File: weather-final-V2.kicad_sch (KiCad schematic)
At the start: 41 parts, among them J1 Conn_02x04_Odd_Even, J2 Conn_01x06_Pin, J3 PROGRAMMING_CONN, J4 USB_C_Receptacle_PowerOnly_6P, U1 AMS1117-5.0, U2 ATmega328-P, Y1 Crystal

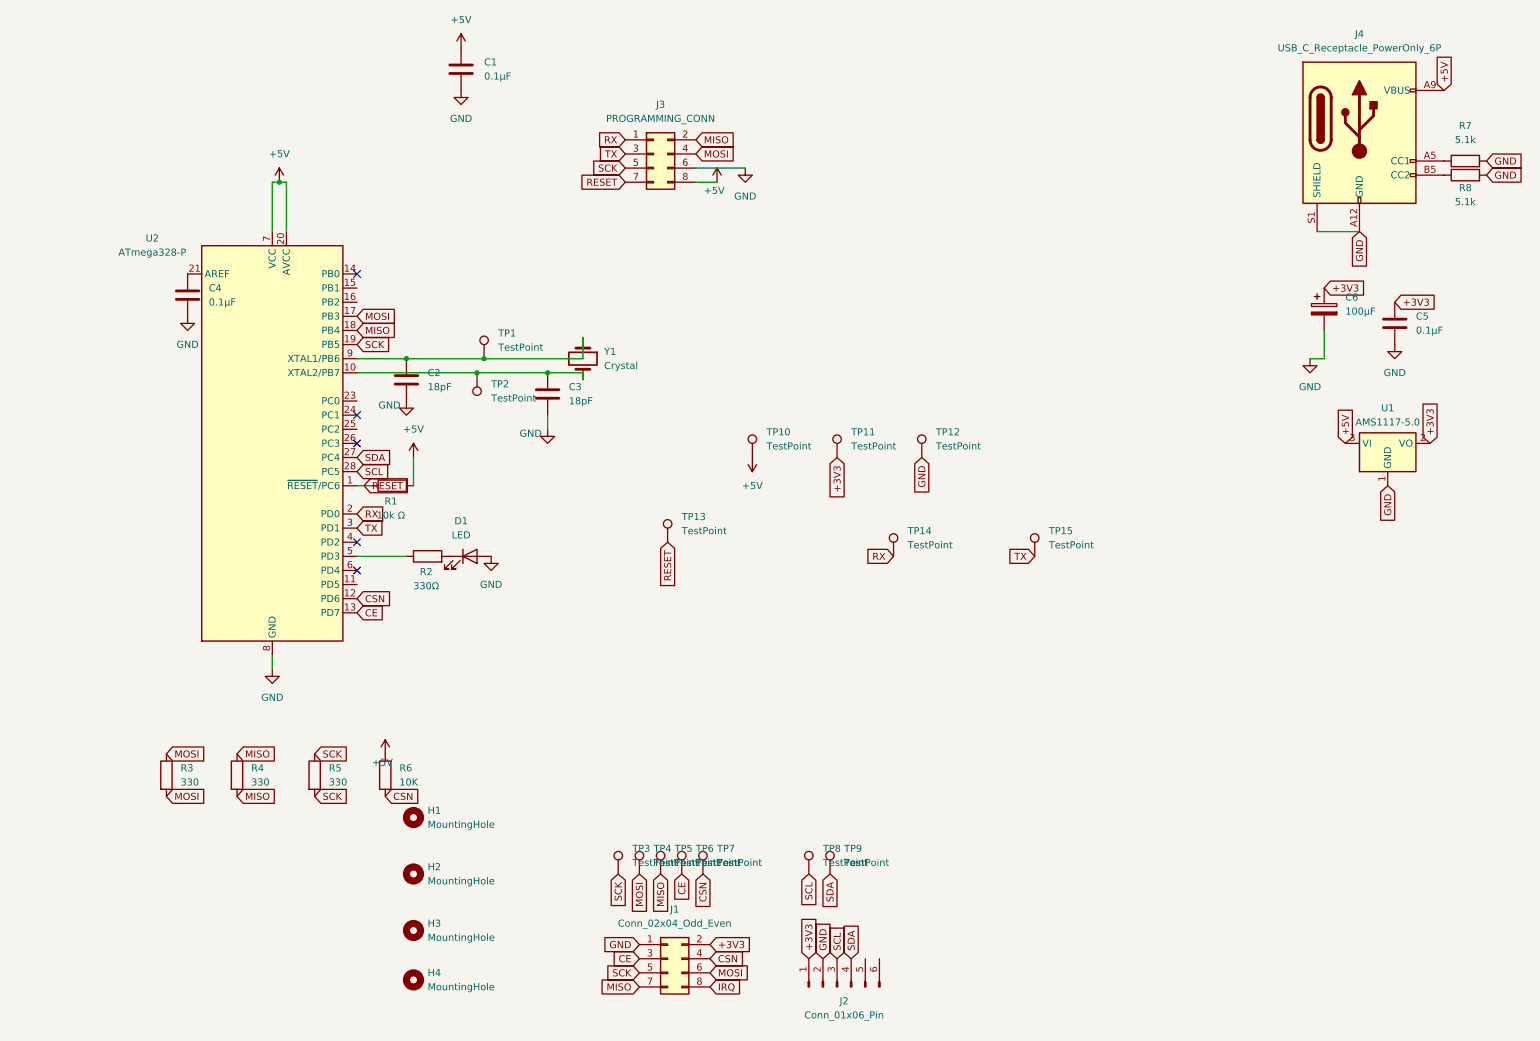
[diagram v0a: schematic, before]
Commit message: Add i2c pullups Clean unnecessary trace widths Add diode for reverse voltage protection on J3 input
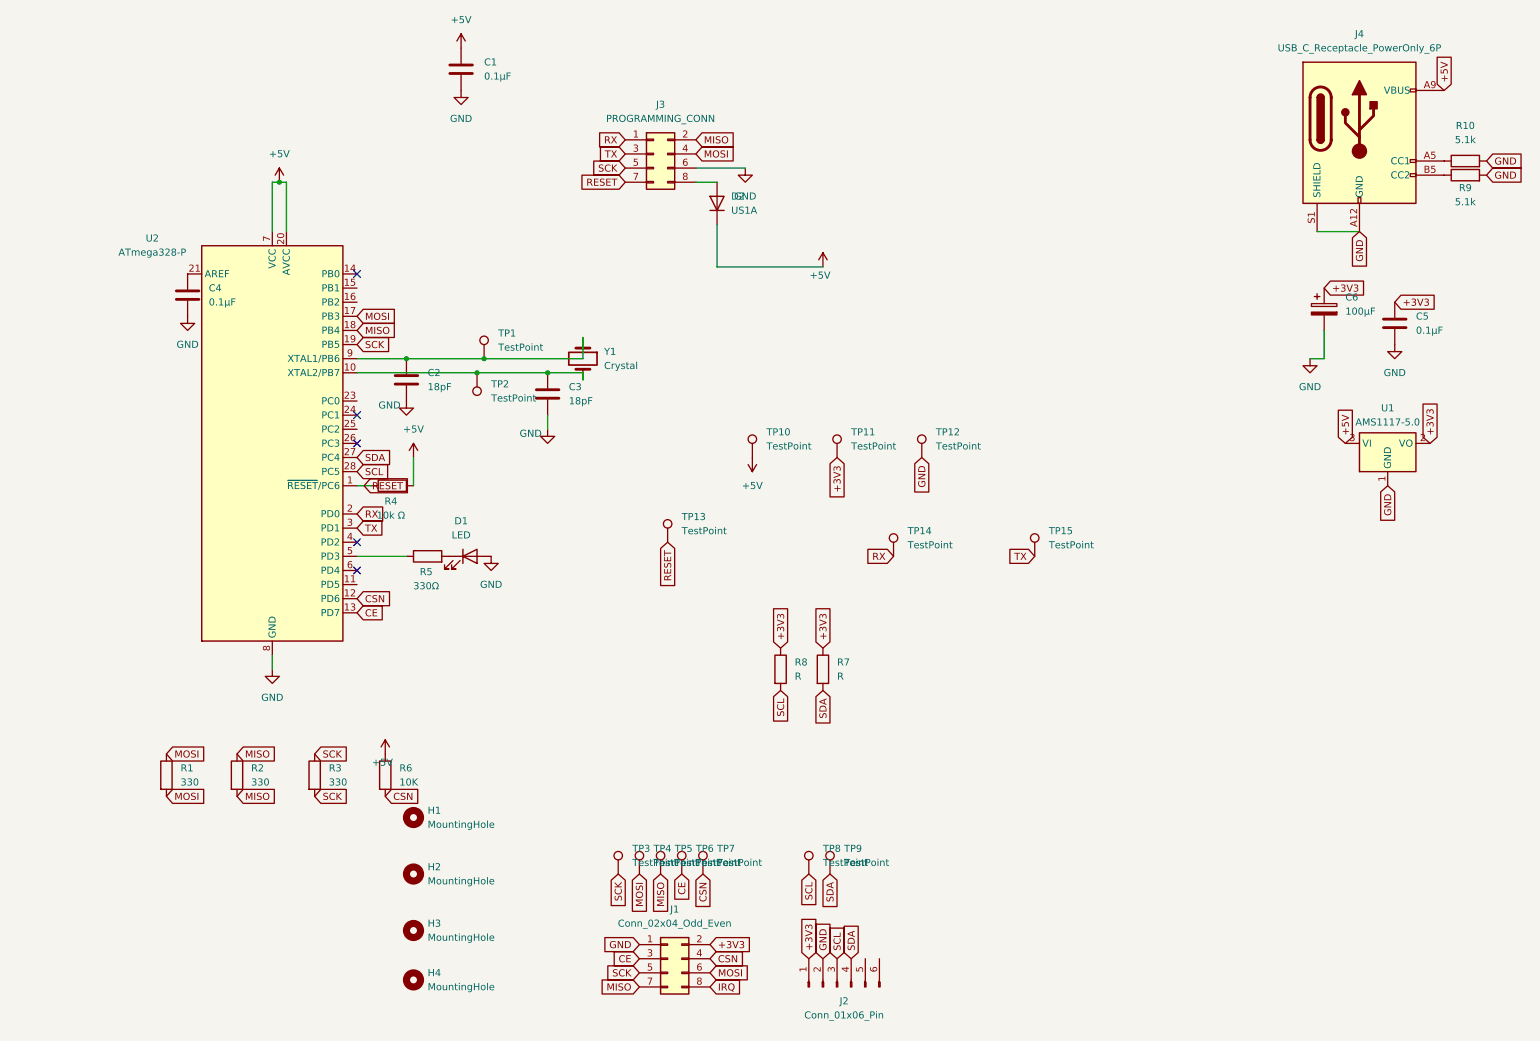
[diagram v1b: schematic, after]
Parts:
- added D2: US1A, Diode_SMD:D_SMA, symbol Diode:US1A
- added R7, R8: R, Resistor_SMD:R_1206_3216Metric_Pad1.30x1.75mm_HandSolder, symbol Device:R
- renumbered R3 to R1, R7 to R10, R4 to R2, R5 to R3, R1 to R4, R2 to R5, R8 to R9
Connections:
- net +3V3: now also R7.1, R8.1
- net +5V: now also D2.1 (K); no longer J3.8 (Pin_8)
- net SCL: now also R8.2
- net SDA: now also R7.2
- new net: D2.2 (A), J3.8 (Pin_8)

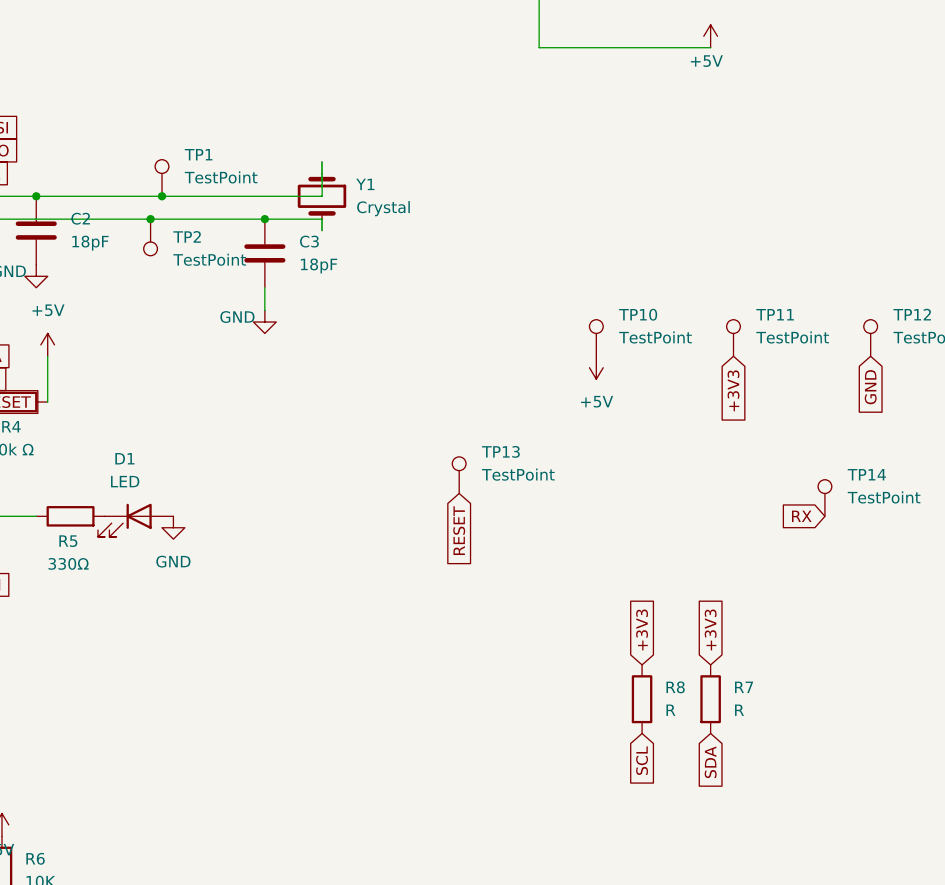
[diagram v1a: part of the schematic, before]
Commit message: Add i2c pullup resistors' values Fix a silkscreen overlap
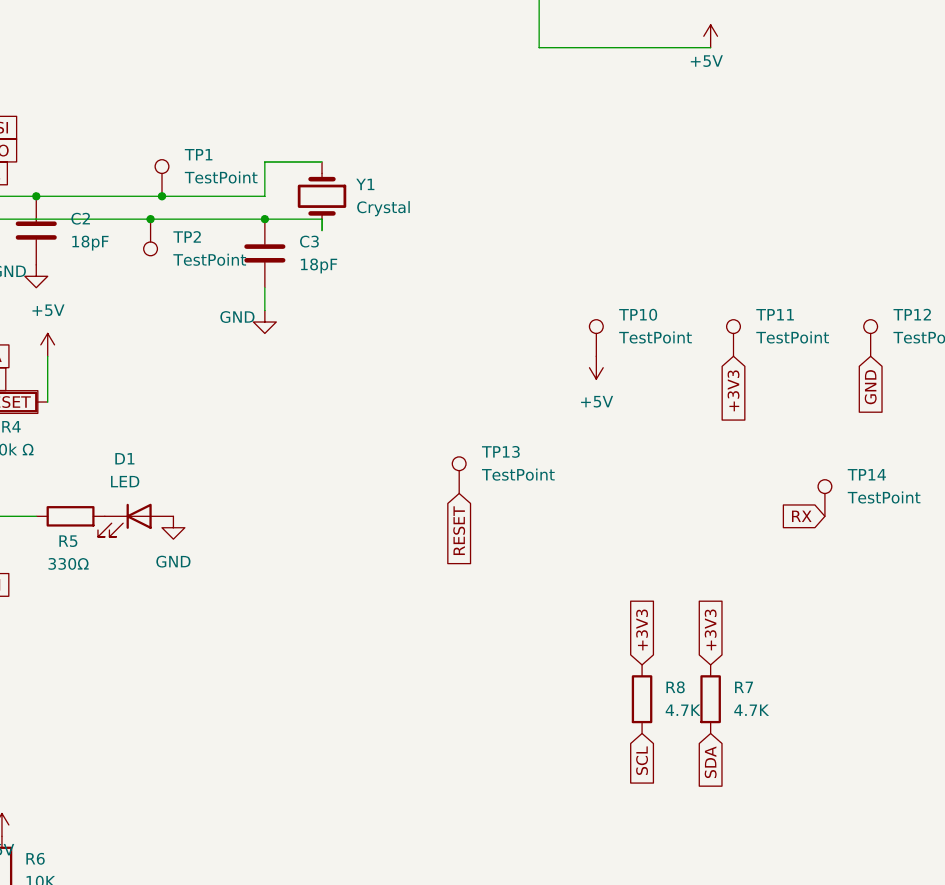
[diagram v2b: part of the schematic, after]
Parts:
- R7, R8: value R -> 4.7K
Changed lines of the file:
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@@
 	(wire
 		(pts
-			(xy 115.57 76.2) (xy 115.57 72.39)
+			(xy 115.57 72.39) (xy 109.22 72.39)
 		)
 		(stroke
@@
 	(wire
 		(pts
-			(xy 97.79 76.2) (xy 115.57 76.2)
+			(xy 109.22 72.39) (xy 109.22 76.2)
 		)
 		(stroke
@@
 	(wire
 		(pts
+			(xy 109.22 76.2) (xy 97.79 76.2)
+		)
+		(stroke
+			(width 0)
+			(type default)
+		)
+	)
+	(wire
+		(pts
 			(xy 247.65 53.34) (xy 255.27 53.34)
 		)
@@
 			)
 		)
-		(property "Value" "R"
+		(property "Value" "4.7K"
 			(at 161.29 133.3499 0)
 			(effects
@@
 			)
 		)
-		(property "Value" "R"
+		(property "Value" "4.7K"
 			(at 153.67 133.3499 0)
 			(effects

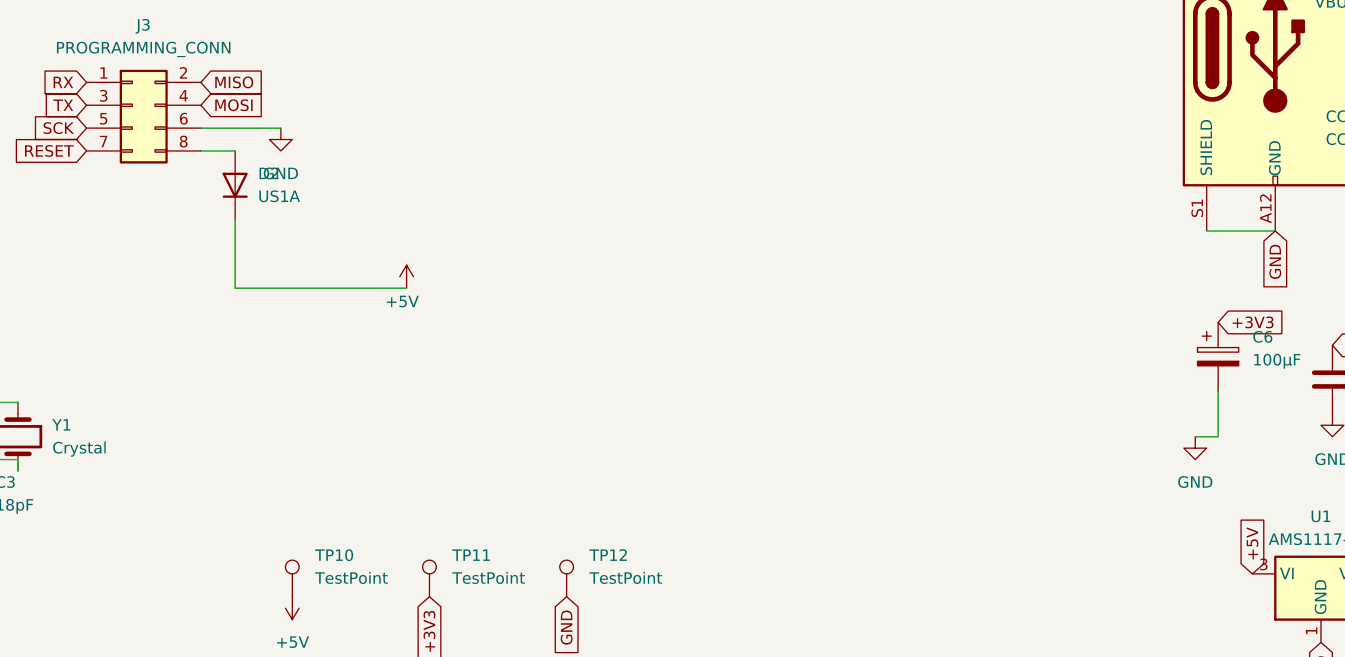
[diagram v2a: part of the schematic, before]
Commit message: Add a 5V power rail decoupling capacitor Add LICENSE and README
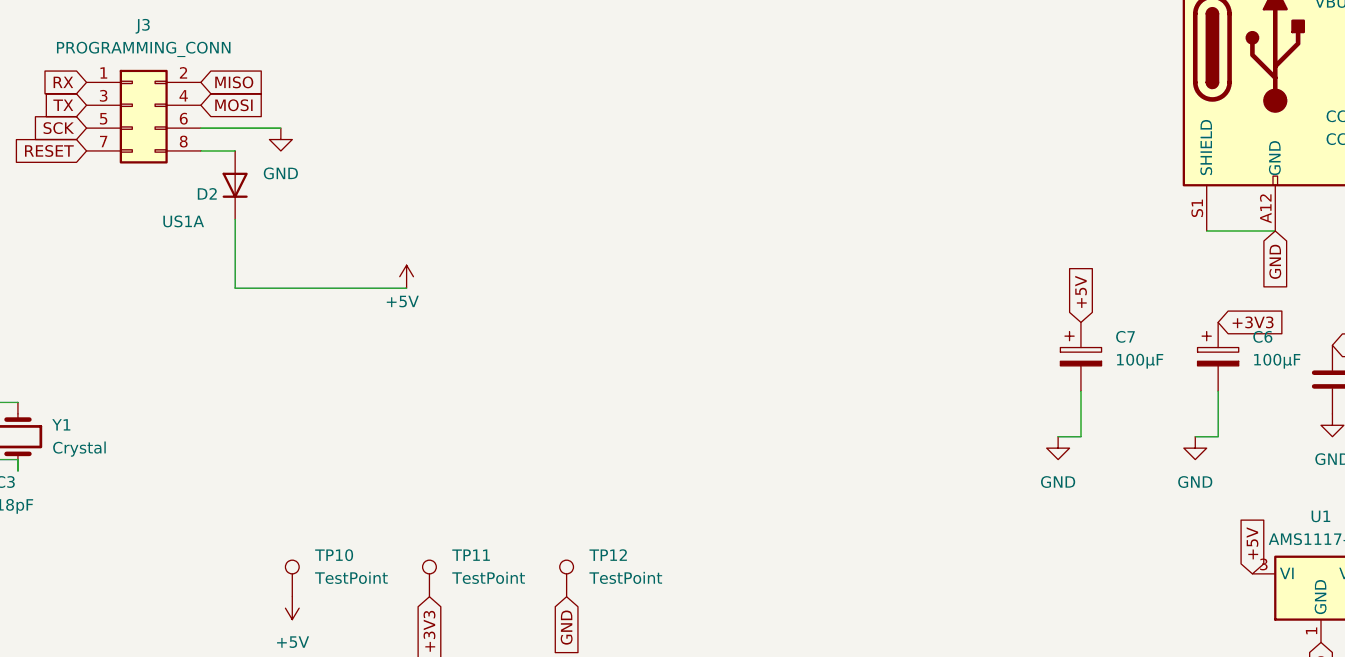
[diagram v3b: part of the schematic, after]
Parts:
- added C7: 100μF, Capacitor_THT:CP_Radial_D5.0mm_P2.00mm, symbol Device:C_Polarized
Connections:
- net +5V: now also C7.1
- net GND: now also C7.2
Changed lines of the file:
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@@
 	(wire
 		(pts
+			(xy 233.68 76.2) (xy 231.14 76.2)
+		)
+		(stroke
+			(width 0)
+			(type default)
+		)
+	)
+	(wire
+		(pts
 			(xy 59.69 132.08) (xy 59.69 129.54)
 		)
@@
 	(wire
 		(pts
+			(xy 233.68 71.12) (xy 233.68 76.2)
+		)
+		(stroke
+			(width 0)
+			(type default)
+		)
+	)
+	(wire
+		(pts
 			(xy 74.93 78.74) (xy 96.52 78.74)
 		)
@@
 		)
 	)
+	(global_label "+5V"
+		(shape input)
+		(at 233.68 63.5 90)
+		(fields_autoplaced yes)
+		(effects
+			(font
+				(size 1.27 1.27)
+			)
+			(justify left)
+		)
+		(property "Intersheetrefs" "${INTERSHEET_REFS}"
+			(at 233.68 56.6443 90)
+			(effects
+				(font
+					(size 1.27 1.27)
+				)
+				(justify left)
+				(hide yes)
+			)
+		)
+	)
 	(global_label "SCK"
 		(shape input)
@@
 	)
 	(symbol
+		(lib_id "power:GND")
+		(at 231.14 76.2 0)
+		(unit 1)
+		(exclude_from_sim no)
+		(in_bom yes)
+		(on_board yes)
+		(dnp no)
+		(fields_autoplaced yes)
+		(property "Reference" "#PWR014"
+			(at 231.14 82.55 0)
+			(effects
+				(font
+					(size 1.27 1.27)
+				)
+				(hide yes)
+			)
+		)
+		(property "Value" "GND"
+			(at 231.14 81.28 0)
+			(effects
+				(font
+					(size 1.27 1.27)
+				)
+			)
+		)
+		(property "Footprint" ""
+			(at 231.14 76.2 0)
+			(effects
+				(font
+					(size 1.27 1.27)
+				)
+				(hide yes)
+			)
+		)
+		(property "Datasheet" ""
+			(at 231.14 76.2 0)
+			(effects
+				(font
+					(size 1.27 1.27)
+				)
+				(hide yes)
+			)
+		)
+		(property "Description" "Power symbol creates a global label with name \"GND\" , ground"
+			(at 231.14 76.2 0)
+			(effects
+				(font
+					(size 1.27 1.27)
+				)
+				(hide yes)
+			)
+		)
+		(pin "1"
+		)
+		(instances
+			(project "weather-final-V2"
+				(path "/eba07791-23f4-411a-9621-29ccfead6e0d"
+					(reference "#PWR014")
+					(unit 1)
+				)
+			)
+		)
+	)
+	(symbol
 		(lib_id "Connector:TestPoint")
 		(at 196.85 111.76 0)
@@
 	)
 	(symbol
+		(lib_id "Device:C_Polarized")
+		(at 233.68 67.31 0)
+		(unit 1)
+		(exclude_from_sim no)
+		(in_bom yes)
+		(on_board yes)
+		(dnp no)
+		(fields_autoplaced yes)
+		(property "Reference" "C7"
+			(at 237.49 65.1509 0)
+			(effects
+				(font
+					(size 1.27 1.27)
+				)
+				(justify left)
+			)
+		)
+		(property "Value" "100μF"
+			(at 237.49 67.6909 0)
+			(effects
+				(font
+					(size 1.27 1.27)
+				)
+				(justify left)
+			)
+		)
+		(property "Footprint" "Capacitor_THT:CP_Radial_D5.0mm_P2.00mm"
+			(at 234.6452 71.12 0)
+			(effects
+				(font
+					(size 1.27 1.27)
+				)
+				(hide yes)
+			)
+		)
+		(property "Datasheet" "~"
+			(at 233.68 67.31 0)
+			(effects
+				(font
+					(size 1.27 1.27)
+				)
+				(hide yes)
+			)
+		)
+		(property "Description" "Polarized capacitor"
+			(at 233.68 67.31 0)
+			(effects
+				(font
+					(size 1.27 1.27)
+				)
+				(hide yes)
+			)
+		)
+		(pin "1"
+		)
+		(pin "2"
+		)
+		(instances
+			(project "weather-final-V2"
+				(path "/eba07791-23f4-411a-9621-29ccfead6e0d"
+					(reference "C7")
+					(unit 1)
+				)
+			)
+		)
+	)
+	(symbol
 		(lib_id "Connector:TestPoint")
 		(at 125.73 168.91 0)
@@
 		(on_board yes)
 		(dnp no)
-		(fields_autoplaced yes)
 		(property "Reference" "D2"
-			(at 142.24 46.9899 90)
+			(at 135.382 49.276 90)
 			(effects
 				(font
@@
 		)
 		(property "Value" "US1A"
-			(at 142.24 49.5299 90)
+			(at 131.572 52.324 90)
 			(effects
 				(font
